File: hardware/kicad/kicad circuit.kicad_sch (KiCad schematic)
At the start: 41 parts, among them J1 Screw_Terminal_01x05, J2 Screw_Terminal_01x06, J3 XT60 30A cont./60A surge, U1 36V 無線充電模組, U10 DB9 to USB, U11 HC-SR04P (3-5.5V), U12 HC-SR04P (3-5.5V), U13 HC-SR04P (3-5.5V), U14 HC-SR04P (3-5.5V), U15 HC-SR04P (3-5.5V), U16 HC-SR04P (3-5.5V), U17 HC-SR04P (3-5.5V), U18 HC-SR04P (3-5.5V), U2 36V 無線充電模組, U3 XL4016 CC/CV, U4 XL4016 CC/CV, U5 XL4016 CV only, U6 INA226 (R100 removed), U7 AGV-BLD-2S, U8 jetson orin nx, U9 A2M12

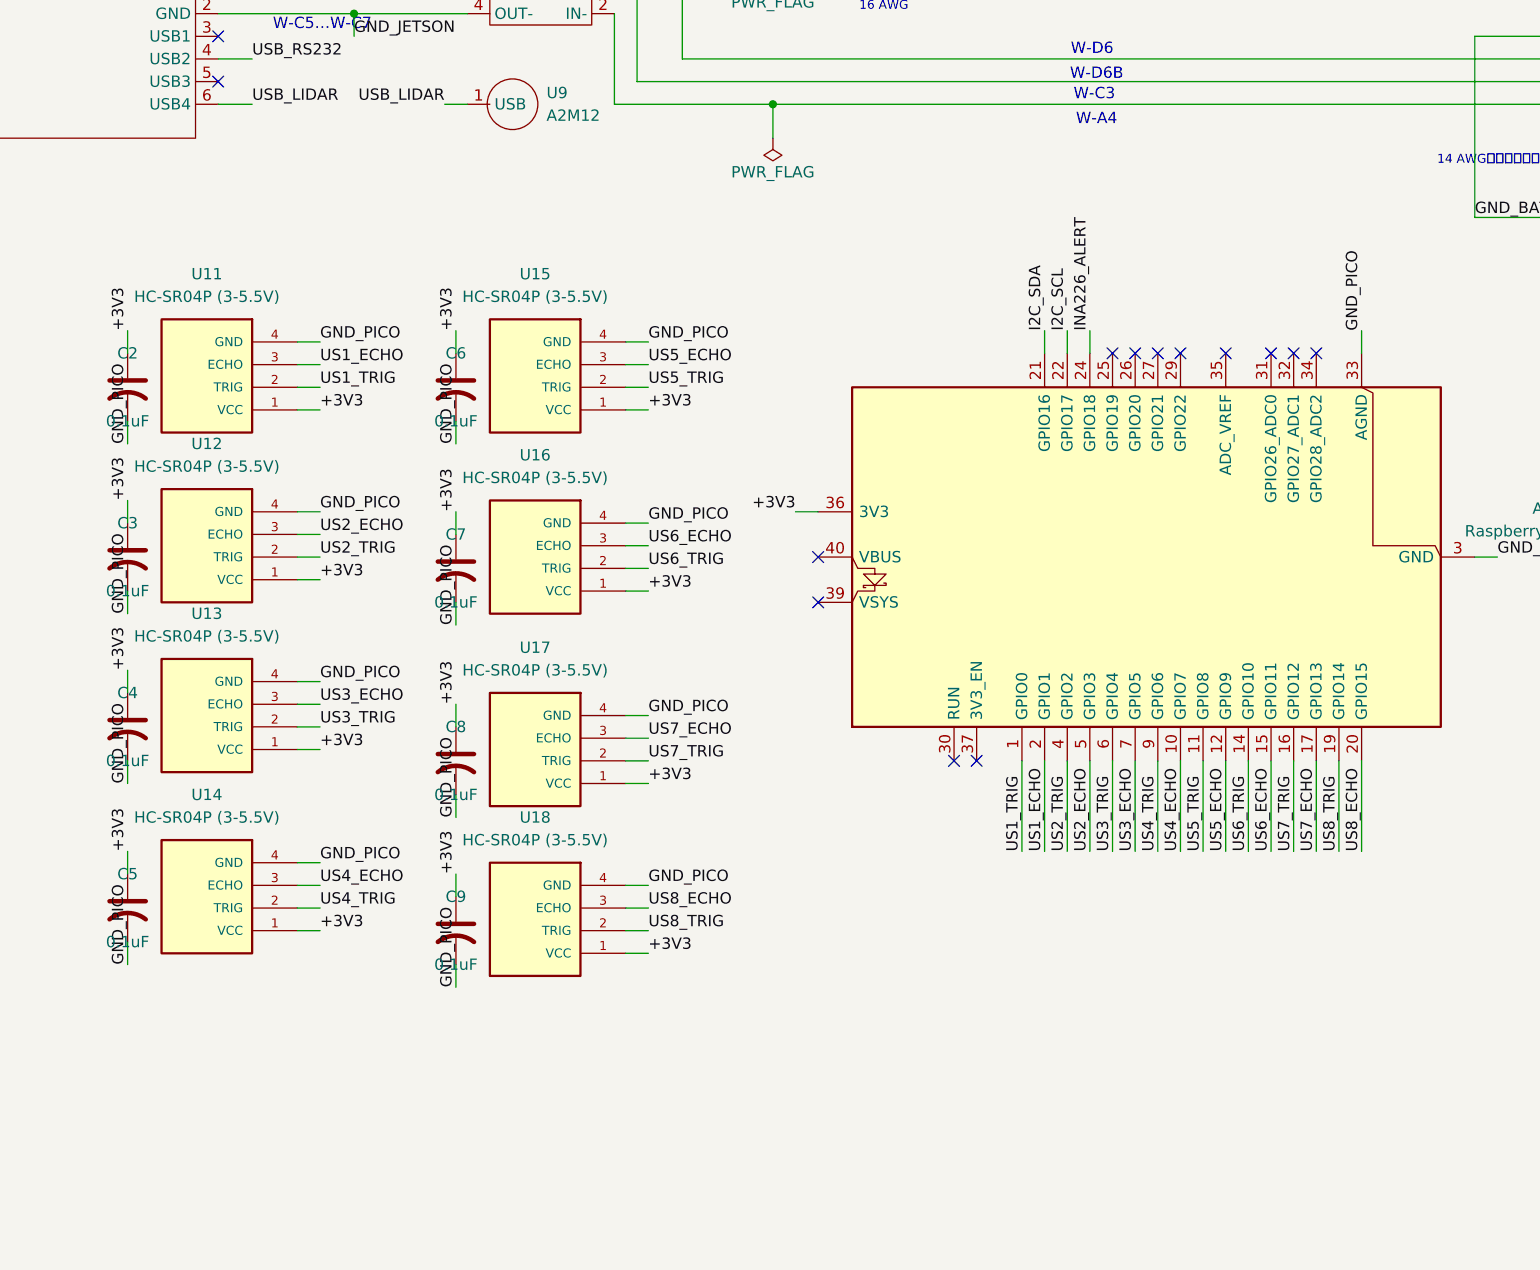
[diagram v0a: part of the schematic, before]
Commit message: hardware(kicad): 同步 BNO055/J4 接線並改用專案相對路徑符號庫
把 repo 鏡像從第八輪拉齊到 Win11 上第十輪的狀態：新增 BNO055（U19）、
Jetson 40-pin 排針（J4）、#PWR005，以及 JET_3V3／JET_I2C_SDA／JET_I2C_SCL
三條網路。原理圖與網表為 Win11 專案目錄原樣複製，未經任何文字編輯。

sym-lib-table 的 HC-SR04 條目改用 ${KIPRJMOD}/HC-SR04.kicad_sym 相對路徑，
取代原本指向 OneDrive 的絕對路徑，讓符號庫隨專案自足、不再依賴特定機器的
使用者目錄。Win11 端已同步為同一份 sym-lib-table（SHA256 相同），
且 HC-SR04.kicad_sym 已複製到專案根與 repo 鏡像同位置。
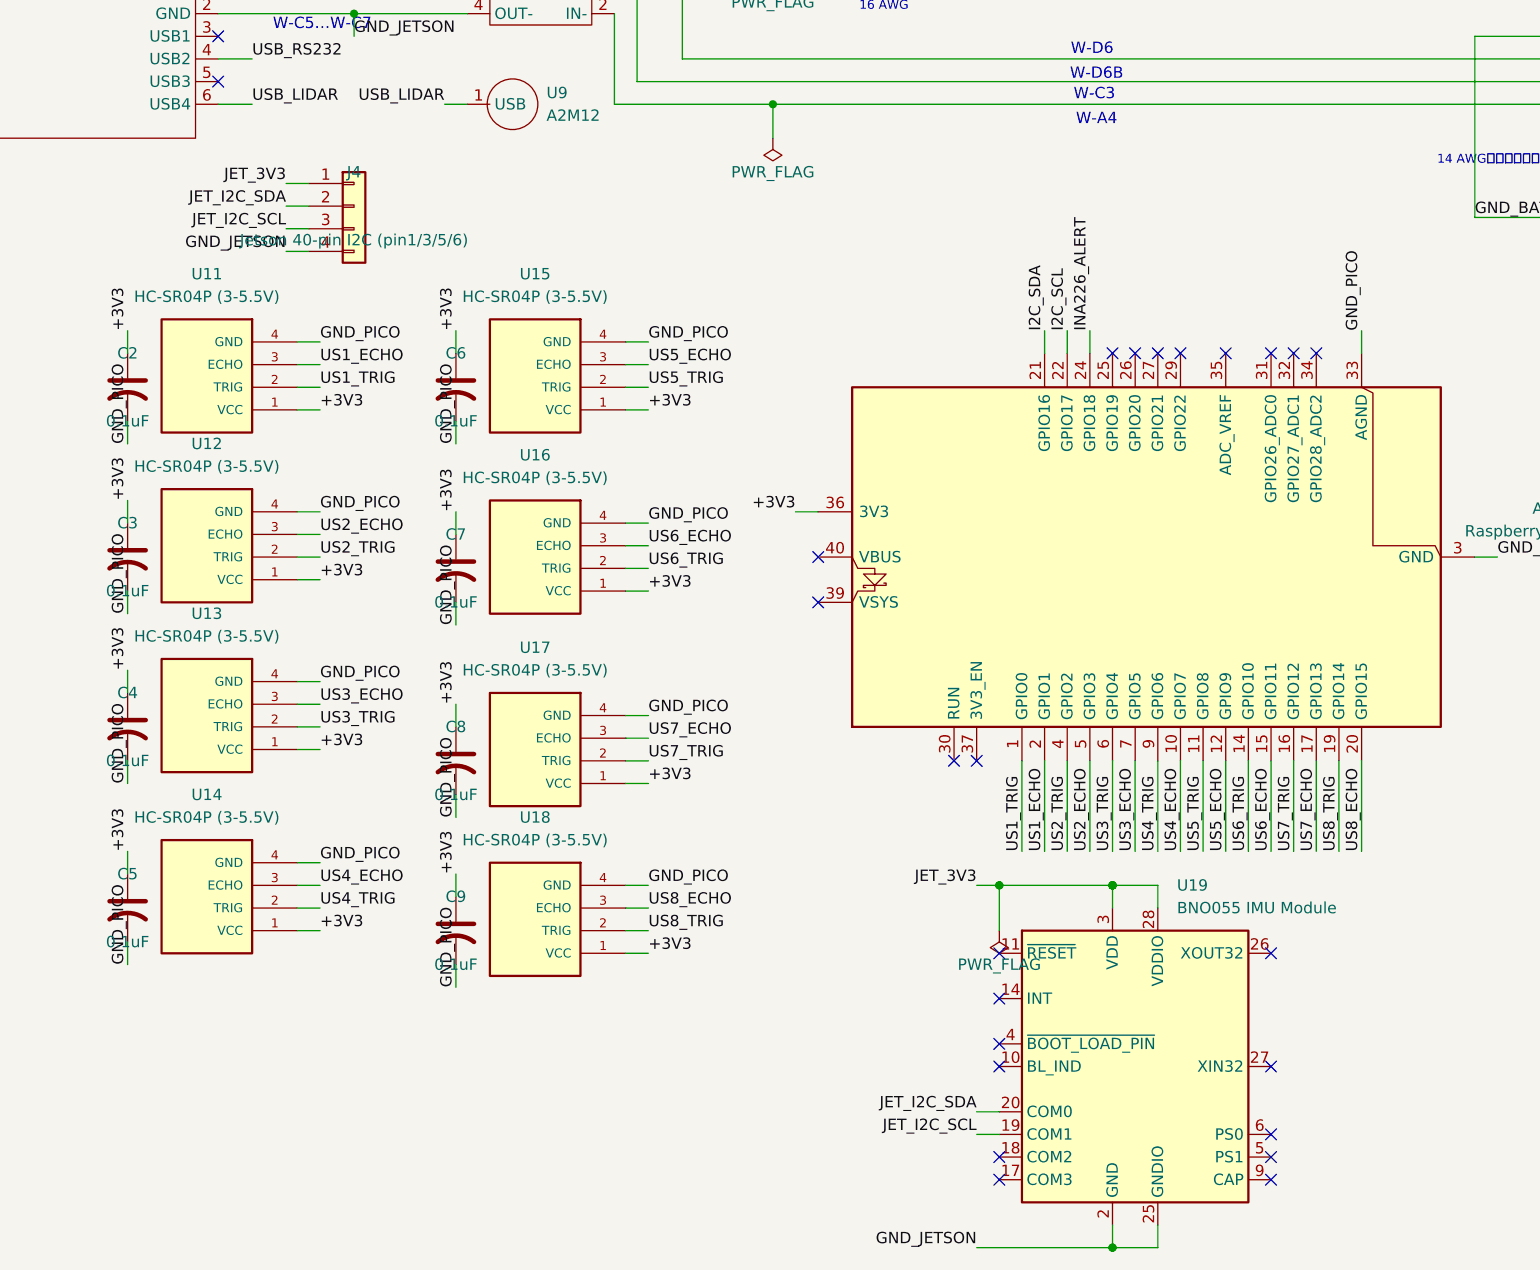
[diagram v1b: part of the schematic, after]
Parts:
- added J4: Jetson 40-pin I2C (pin1/3/5/6), symbol Connector_Generic:Conn_01x04
- added U19: BNO055 IMU Module, Package_LGA:LGA-28_5.2x3.8mm_P0.5mm, symbol Sensor_Motion:BNO055
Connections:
- net GND_JETSON: now also J4.4 (Pin_4), U19.2 (GND), U19.25 (GNDIO)
- new net JET_3V3: J4.1 (Pin_1), U19.28 (VDDIO), U19.3 (VDD)
- new net JET_I2C_SCL: J4.3 (Pin_3), U19.19 (COM1)
- new net JET_I2C_SDA: J4.2 (Pin_2), U19.20 (COM0)
- no-connect marks 14 -> 25

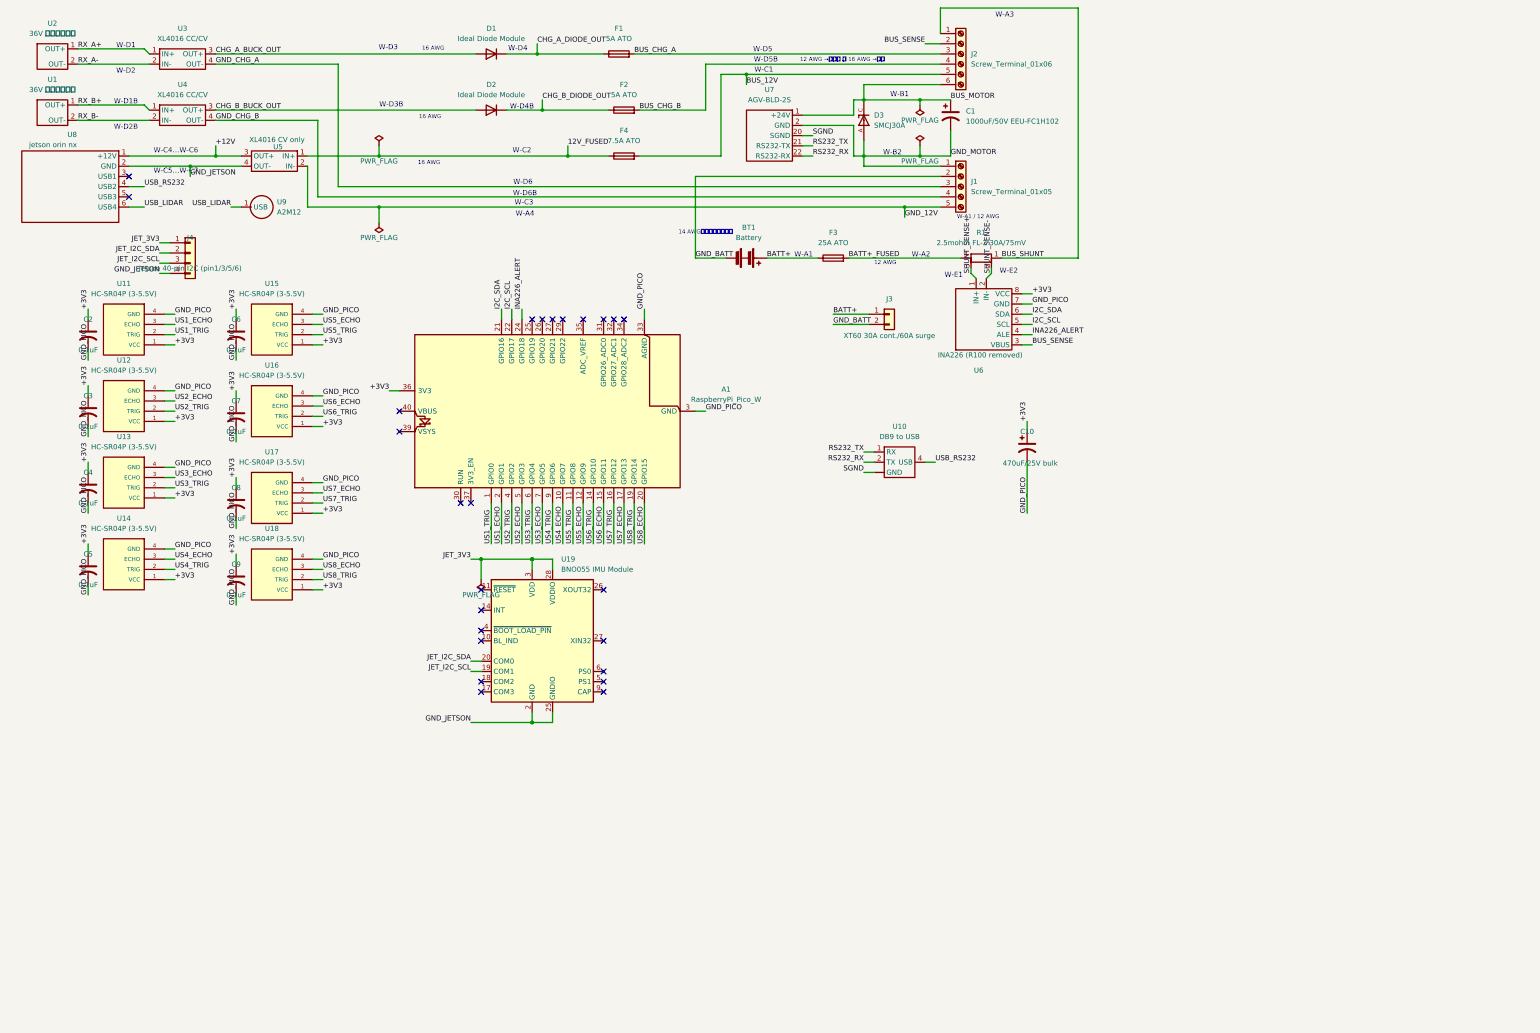
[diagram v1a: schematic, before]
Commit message: hardware(kicad): 原理圖送審版 v1.0（ERC 歸零、A3 圖框、標題欄）
移除 USB_PICO 上多餘的 PWR_FLAG 與 A1.VBUS 的 no-connect 旗標，清掉
J8／R2 五處線端點空接（label 改貼 stub 末端，網路成員不變），並修正
分流器區 R1 規格文字與 SHUNT_SENSE± 標籤重疊。

圖框由 A4 改為 A3，標題欄補上 AMR 電路配置／v1.0／2026-08-04。
另加圖面說明，記載兩筆 ERC 例外的理由：U7 SGND 與 U10 GND 相接為
驅動器手冊 §1.3 記載的既有地迴路（緩解見 §7）；Pico GND 與 AGND
模組內部本即相通。兩者皆為符號腳位型別造成的假警報，接線正確。

kicad-cli sch erc: 0 errors / 16 warnings
（14 筆封裝庫未註冊、1 筆 BT1 符號 metadata、1 筆 Pico 腳位型別）
具名網路 61 條，與修改前相同。

註：.kicad_sch 的大量 diff 多為 KiCad 重新序列化造成的縮排變動，
非設計變更。

Claude-Session: https://claude.ai/code/session_013miYUCpfh3nvAFYDPWKqDN
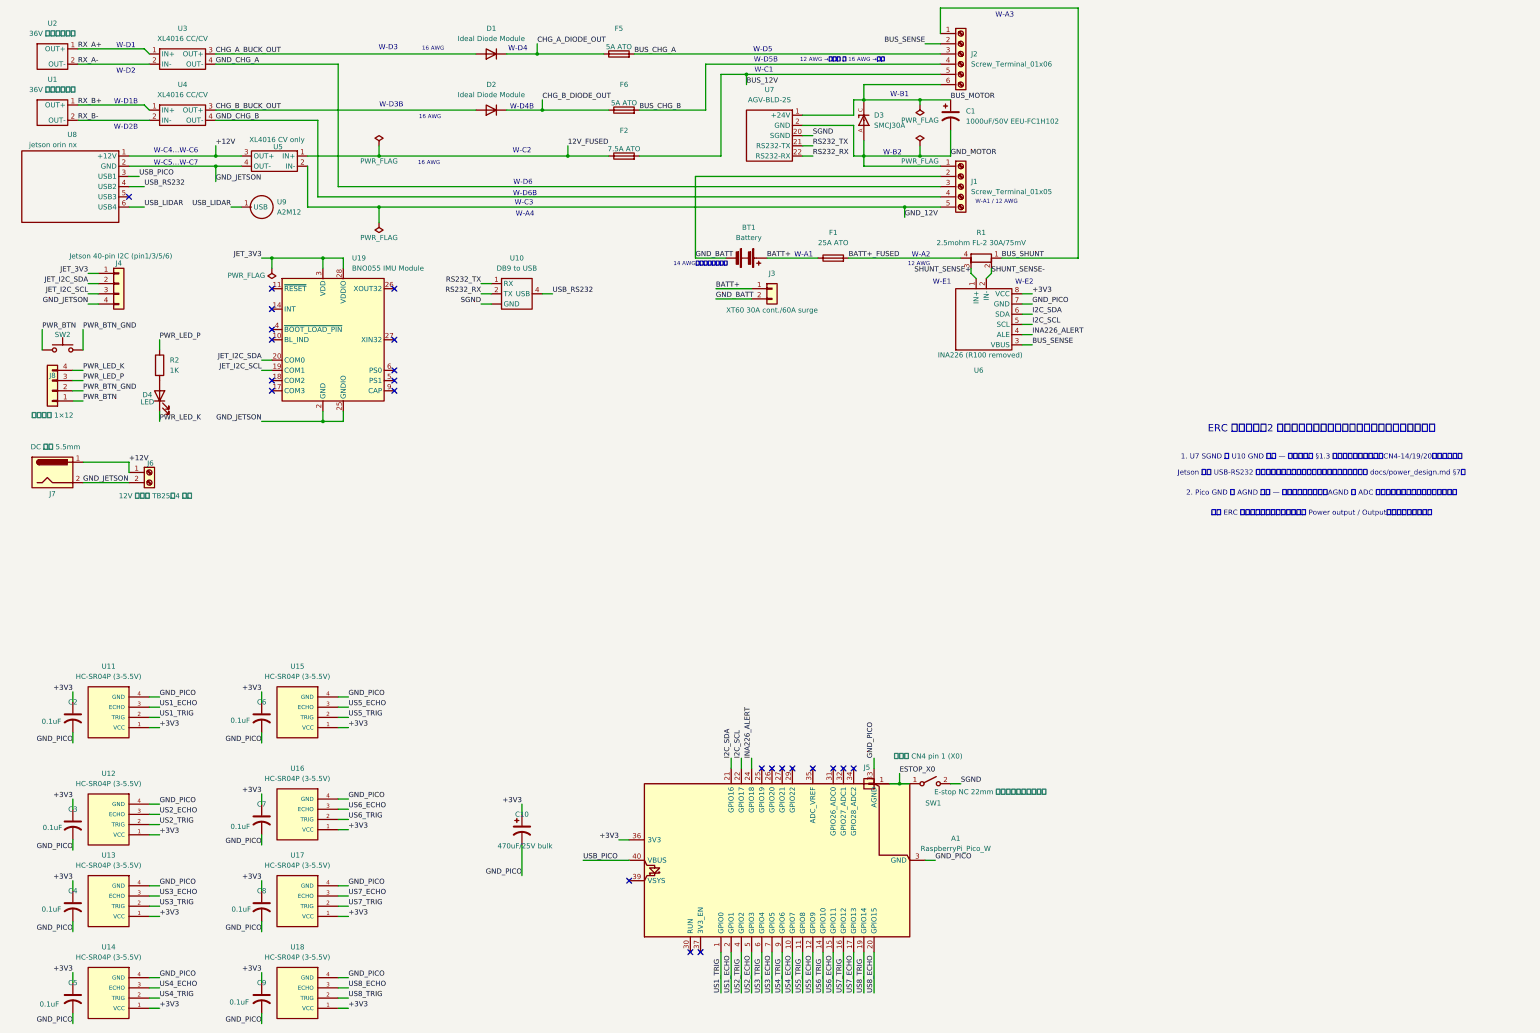
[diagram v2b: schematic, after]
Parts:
- added D4: LED, symbol Device:LED
- added J5: 驅動器 CN4 pin 1 (X0), symbol Connector_Generic:Conn_01x01
- added J6: 12V 端子台 TB25（4 位）, symbol Connector:Screw_Terminal_01x02
- added J7: DC 插頭 5.5mm, symbol Connector:Barrel_Jack
- added J8: 載板排針 1×12, symbol Connector_Generic:Conn_01x04
- added R2: 1K, symbol Device:R
- added SW1: E-stop NC 22mm 蘑菇頭（常閉自保持）, symbol Switch:SW_SPST
- added SW2: 4 pin tactile（內部兩兩相通，須以電表確認選對腳）, symbol Switch:SW_Push
- renumbered F3 to F1, F4 to F2, F1 to F5, F2 to F6
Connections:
- net +12V: now also J6.1 (Pin_1), J7.1
- net GND_JETSON: now also J6.2 (Pin_2), J7.2
- net SGND: now also SW1.2 (B)
- net USB_PICO: now reaches A1.40 (VBUS)
- net USB_PICO: now also U8.3 (USB1)
- new net: D4.2 (A), R2.2
- new net ESTOP_X0: J5.1 (Pin_1), SW1.1 (A)
- new net PWR_BTN: J8.1 (Pin_1), SW2.1
- new net PWR_BTN_GND: J8.2 (Pin_2), SW2.2
- new net PWR_LED_K: D4.1 (K), J8.4 (Pin_4)
- new net PWR_LED_P: J8.3 (Pin_3), R2.1
- no-connect marks 25 -> 23
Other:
- note added: "1. U7 SGND 與 U10 GND 相接 — 驅動器手冊 §1.3 明示電源地與信號地（CN4-14/19/20）內部相通；"
- note added: "2. Pico GND 與 AGND 相接 — 模組內部本即相通，AGND 為 ADC 參考地，外部共地是原廠標準接法。"
- note added: "ERC 例外說明（2 筆，均為符號腳位型別造成的假警報，接線正確）"
- note added: "Jetson 地經 USB-RS232 連至動力地，為既有且已知的地迴路，緩解措施見 docs/power_design.md §7。"
- note added: "兩者 ERC 報錯僅因符號將接地腳宣告為 Power output / Output，與實際接線無關。"
- company: (none) -> 愛吠的狗機器人
- title: (none) -> AMR 電路配置
- moved on the sheet: A1, C10, C2, C3, C4, C5, C6, C7, C8, C9, J3, J4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

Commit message: hardware(kicad): 車端充電輸入由無線改為接觸式刷塊
拆除無線充電整段：U1/U2（36V 無線接收模組）、U3/U4（XL4016 CC/CV）、
D2/F6（B 腿防倒灌與保險絲），充電器職責移至 dock 端（HLG-150H-30A，
28.0V/5A CC，見 docs/charging_dock_design.md）。

新增接觸式輸入鏈：J9 刷塊端子台 → D1 理想二極體（防倒灌，依 dock 文件
§9.1 車端必要項）→ F5 保險絲 → J2 正極匯流排；刷塊⊖ 經 J1 星點回流
（沿用原充電 OUT− 位）。充電電流經 R1 分流器反向流入，INA226 讀負電流，
「>2A＝充電中」判定（T21）不受影響。

F5 額定 5A → 7.5A ATO（充電 5A CC × 1.5 裕度，且低於 dock 端 F-D1 15A，
故障時車端先斷）。網路更名去除雙腿殘留：BUS_CHG_A → BUS_CHG、
CHG_A_DIODE_OUT → CHG_DIODE_OUT；新增 BRUSH_P／BRUSH_N。
J1.4／J2.4 空出的端子位加 no-connect 旗標。

kicad-cli sch erc: 0 errors / 11 warnings（9 筆封裝庫未註冊、BT1 符號
metadata、Pico 腳位型別——皆為既有已解釋項）。網路數 61 → 53。
W-D4／W-D5 線號因鏈路段落未變而繼續有效；刷塊兩條新線的線號待接線
清單文件補充。

Claude-Session: https://claude.ai/code/session_013miYUCpfh3nvAFYDPWKqDN
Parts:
- removed D2: Ideal Diode Module, symbol Device:D
- removed F6: 5A ATO, symbol Device:Fuse
- removed U1, U2: 36V 無線充電模組, module, symbol Wireless Charging Module:Wireless_Charging_Module
- removed U3, U4: XL4016 CC/CV, module, symbol Buck Converter:XL4016_CV_module
- added J9: 車端刷塊引線（⊕上/⊖下）, symbol Connector:Screw_Terminal_01x02
- F5: value 5A ATO -> 7.5A ATO
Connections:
- net BUS_CHG_A renamed BUS_CHG
- net BUS_CHG_B: no longer names the net of J2.4 (Pin_4)
- net CHG_A_BUCK_OUT renamed BRUSH_P
- net BRUSH_P: now also J9.1 (Pin_1)
- net CHG_A_DIODE_OUT renamed CHG_DIODE_OUT
- net GND_CHG_A renamed BRUSH_N
- net BRUSH_N: now also J9.2 (Pin_2)
- net GND_CHG_B: no longer names the net of J1.4 (Pin_4)
- no-connect marks 23 -> 25
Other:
- note removed: "W-C3"
- note removed: "W-D1"
- note removed: "W-D1B"
- note removed: "W-D2"
- note removed: "W-D2B"
- note removed: "W-D3"
- note removed: "W-D3B"
- note removed: "W-D4B"
- note removed: "W-D5B"
- note removed: "W-D6"
- note removed: "W-D6B"
- moved on the sheet: BT1, F1, F2, J3, R1, U5, U6, U8, U9
